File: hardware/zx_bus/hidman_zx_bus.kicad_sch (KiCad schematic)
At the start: 56 parts, among them J1 X1A, J10 JOY_ENABLE, J11 TAPE IN, J12 USB EXT, J13 PS/2 Mouse External Bracket, J14 PS/2 Keyboard External Bracket, J2 X1B, J3 UART, J4 USB_A, J5 USB_A, J6 Keyboard, J7 Mouse / Key, J8 GOTEK, J9 JTAG, Q1 BSS123, Q2 BSS123, Q3 BSS123, SW1 RESET, SW2 BOOT0, U1 CH559L, U2 EPM3128ATC100, U3 AMS1117-3.3, U4 74LVC1G125DB, U6 IP4220CZ6, Y1 12MHz

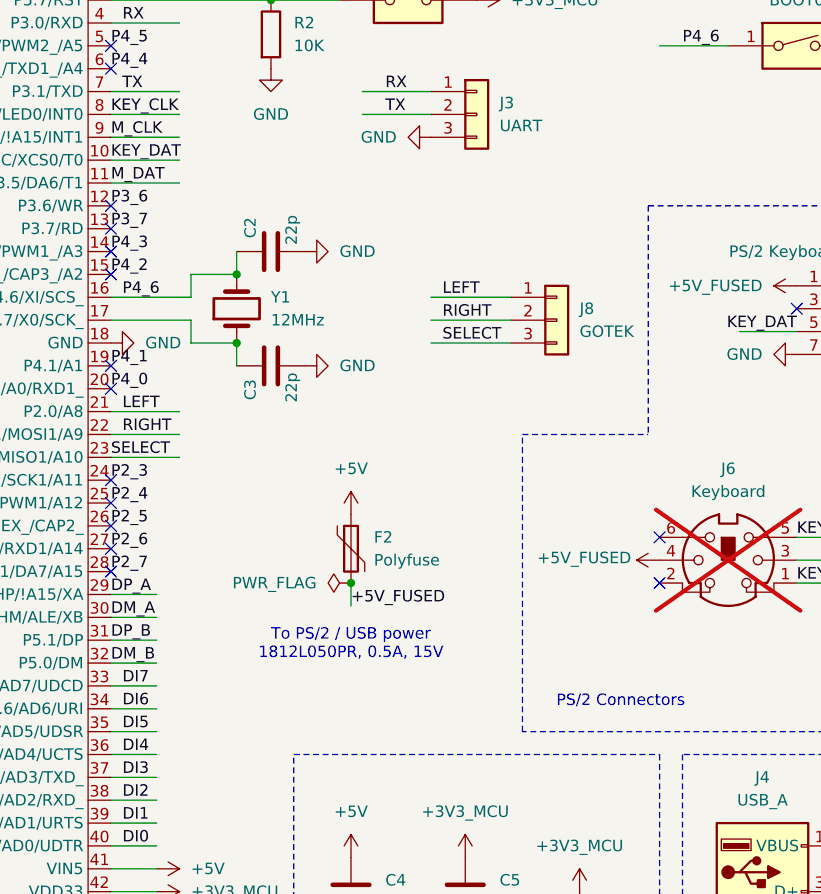
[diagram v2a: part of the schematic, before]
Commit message: Replace 1812 polyfuse Littelfuse 1812L050PR (0.5A, 15V) with 1206 Bourns MF-NSMF075-2 (0.75A, 6V). Add schematic comments about CH559L omitted reset and external clock components.
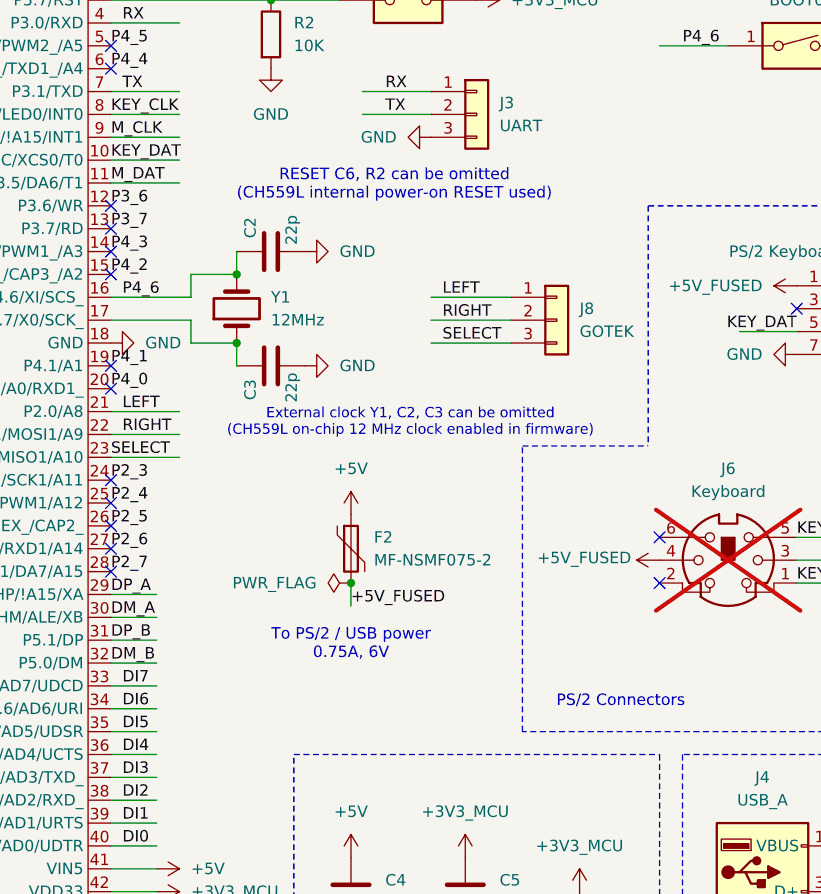
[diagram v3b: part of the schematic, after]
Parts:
- F2: value Polyfuse -> MF-NSMF075-2; footprint Fuse:Fuse_1812_4532Metric_Pad1.30x3.40mm_HandSolder -> Fuse:Fuse_1206_3216Metric_Pad1.42x1.75mm_HandSolder
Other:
- note added: "External clock Y1, C2, C3 can be omitted (CH559L on-chip 12 MHz clock enabled in firmware)"
- note added: "RESET C6, R2 can be omitted (CH559L internal power-on RESET used)"
- note added: "To PS/2 / USB power 0.75A, 6V"
- note removed: "To PS/2 / USB power 1812L050PR, 0.5A, 15V"
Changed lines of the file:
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@@
 	(polyline
 		(pts
-			(xy 123.19 50.8) (xy 123.19 76.2)
+			(xy 123.19 50.8) (xy 123.19 77.47)
 		)
 		(stroke
@@
 	(polyline
 		(pts
-			(xy 109.22 109.22) (xy 109.22 76.2)
+			(xy 109.22 109.22) (xy 109.22 77.47)
 		)
 		(stroke
@@
 	(polyline
 		(pts
-			(xy 109.22 76.2) (xy 123.19 76.2)
+			(xy 109.22 77.47) (xy 123.19 77.47)
 		)
 		(stroke
@@
 		)
 	)
+	(text "External clock Y1, C2, C3 can be omitted\n(CH559L on-chip 12 MHz clock enabled in firmware)"
+		(exclude_from_sim no)
+		(at 96.774 74.93 0)
+		(effects
+			(font
+				(size 1.143 1.143)
+			)
+		)
+	)
 	(text "USB Interface"
 		(exclude_from_sim no)
@@
 		)
 	)
+	(text "RESET C6, R2 can be omitted\n(CH559L internal power-on RESET used)"
+		(exclude_from_sim no)
+		(at 94.996 48.514 0)
+		(effects
+			(font
+				(size 1.27 1.27)
+			)
+		)
+	)
 	(text "CPLD JTAG Interface"
 		(exclude_from_sim no)
@@
 		)
 	)
-	(text "To PS/2 / USB power\n1812L050PR, 0.5A, 15V"
+	(text "To PS/2 / USB power\n0.75A, 6V"
 		(exclude_from_sim no)
 		(at 90.17 99.568 0)
@@
 			)
 		)
-		(property "Value" "Polyfuse"
+		(property "Value" "MF-NSMF075-2"
 			(at 92.71 90.1699 0)
 			(effects
@@
 			)
 		)
-		(property "Footprint" "Fuse:Fuse_1812_4532Metric_Pad1.30x3.40mm_HandSolder"
+		(property "Footprint" "Fuse:Fuse_1206_3216Metric_Pad1.42x1.75mm_HandSolder"
 			(at 91.44 93.98 0)
 			(effects

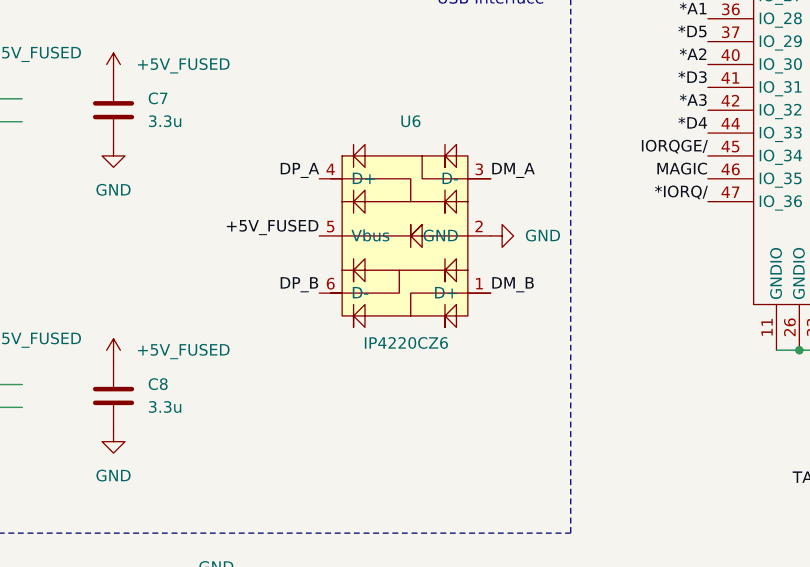
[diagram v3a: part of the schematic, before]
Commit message: Fixed IP4220CZ6 ESD protection IC DM_B/DP_B connections.
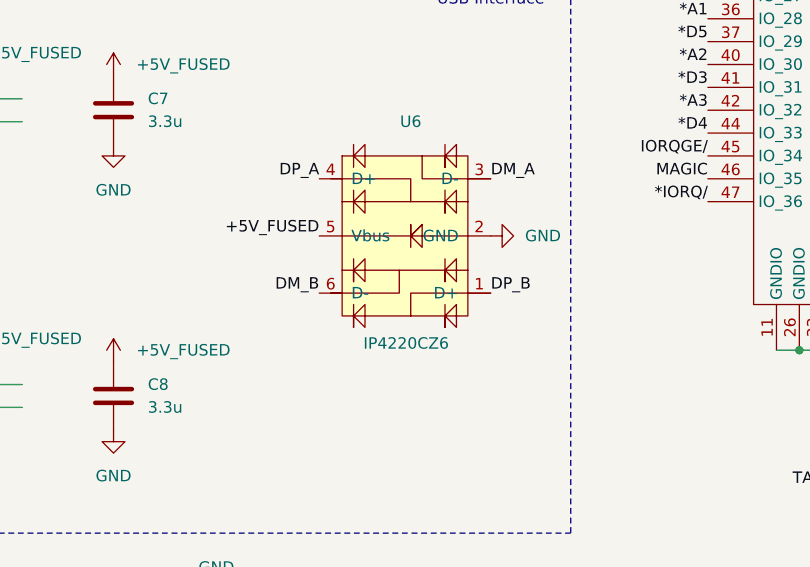
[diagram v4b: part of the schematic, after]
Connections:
- net DM_B: now also U6.6 (D-); no longer U6.1 (D+)
- net DP_B: now also U6.1 (D+); no longer U6.6 (D-)
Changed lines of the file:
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@@
 		)
 	)
-	(label "DP_B"
+	(label "DM_B"
 		(at 184.15 148.59 180)
 		(fields_autoplaced yes)
@@
 		)
 	)
-	(label "DM_B"
+	(label "DP_B"
 		(at 203.2 148.59 0)
 		(fields_autoplaced yes)
